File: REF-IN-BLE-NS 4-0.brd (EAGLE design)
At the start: 44 x 86 mm, 79 parts, among them U1 NRF52832_10QFN48, U2 AEM10941, X1 32 MHz, X2 32.768 kHz

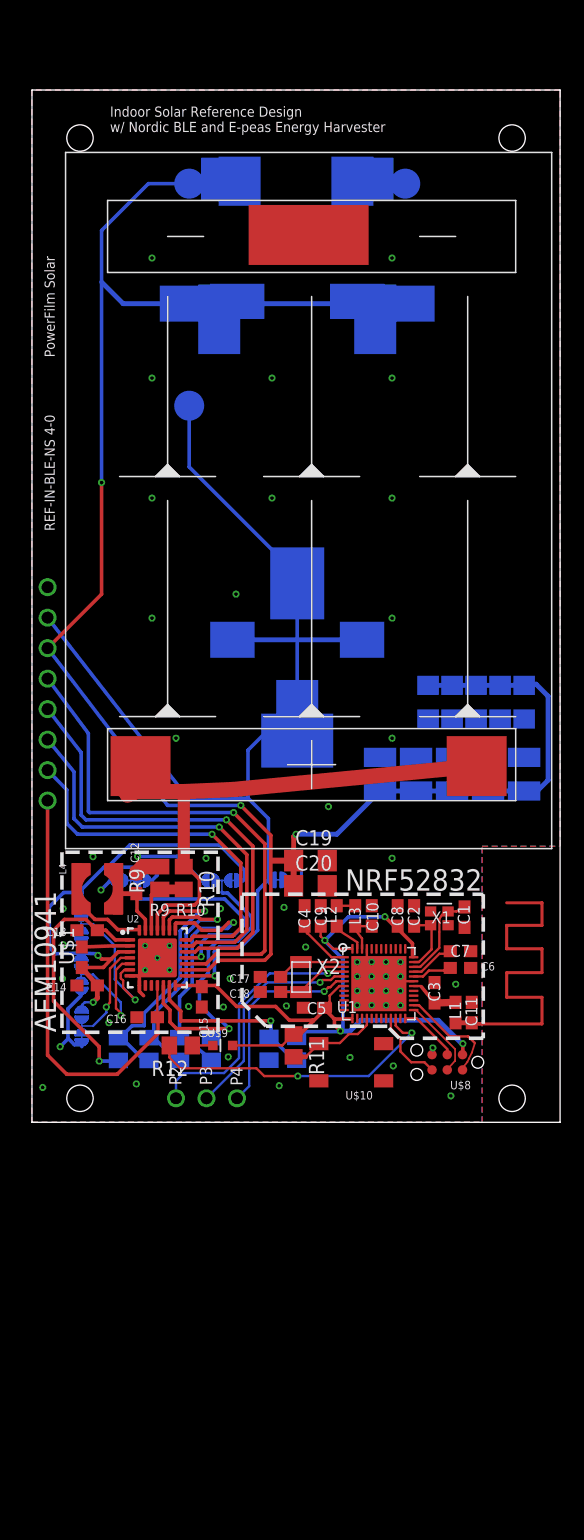
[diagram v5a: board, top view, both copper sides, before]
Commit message: Second revision of board Added LDO bypass circuit to attempt to get a higher efficiency from the charge capacitors. Added a way to break away solar from the rest of the assembly. Moved pin connectors to processing side of the board Swapped 0805 components for 0603 Moved the capacitor bank to the processing side of the board Rerouted some signals to fit everything nicely
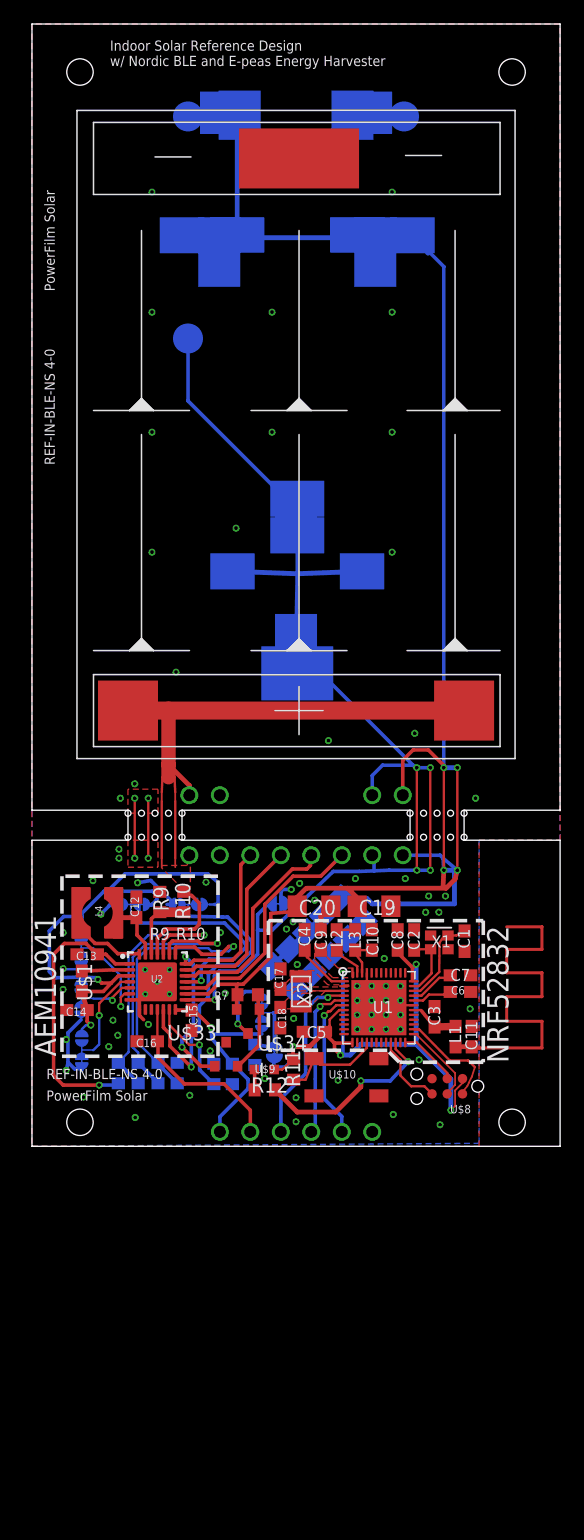
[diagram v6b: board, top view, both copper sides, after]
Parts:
- removed C26, C27, C28, C29, C30: (no value), resistor:C1210
- added R7: 1M, resistor:R0603
- added RTEST: (no value), resistor:R0603
- added U$31: (no value), 00_PF_Nordic:DOUBLE_SOLDER_BRIDGE_1_CLOSED
- added U$32: (no value), 00_PF_Nordic:SOLDER_BRIDGE_CLOSED
- added U$33: DMG2305U-13, 00-PF-DevKits:SOT-23-3-DIODESINC
- added U$34: DMG2302UK-13, 00_PF_Nordic:SOT-23-3-DIODESINC
- added U$35, U$36, U$37, U$38, U$39, U$40, U$41: N/A, 00_PF_Nordic:1MM_PAD
- AE1: value 2.4GHZ_ANTENNA -> N/A
- R1, R2, R3, R4, R5, R6, R9: device resistor:M0805 -> resistor:R0603
- R10, R11, R12: device resistor:R0805 -> resistor:R0603
- U$11: value SOLDER_BRIGDECLOSED -> (none)
- U$12, U$13, U$14, U$15, U$16, U$17, U$18, U$19, U$20, U$21, U$22: value 1MM_PAD -> N/A
- U$2, U$3, U$5, U$6: value DOUBLE_SOLDER_BRIDGE1_CLOSED -> (none)
- U$23: value CAP-XX_A-TYPE -> N/A
- U$24: value CAP-XX_S-TYPE -> N/A
- U$25: value CAP-XX_W-TYPE -> N/A
- U$26: value BZ01_L-TYPE -> N/A
- U$27: value BZ059_N-TYPE -> N/A
- U$28: value BZ01_S-TYPE -> N/A
- U$29: value BZ05_S-TYPE -> N/A
- U$30: value BZ09_S-TYPE -> N/A
- U$4: value DOUBLE_SOLDER_BRIDGE0_CLOSED -> N/A
- U$7: value SOLAR_CELL -> N/A
- U$8: value TC2030-IDC -> N/A
- moved U$18 34.3 mm to (30.9, 24.2)
- moved U$19 33.5 mm to (28.4, 24.2)
- moved U$16 32.4 mm to (18.2, 1.20)
- moved U$12 28.6 mm to (25.8, 24.2)
- moved C21 25.9 mm to (21.0, 14.0), turned to 225 degrees
- moved U$13 25.1 mm to (23.3, 24.2)
- moved C22 25.0 mm to (22.4, 15.4), turned to 225 degrees
- moved C23 24.1 mm to (23.8, 16.9), turned to 225 degrees
- moved C24 23.2 mm to (25.2, 18.3), turned to 225 degrees
- moved U$17 22.5 mm to (15.7, 29.2)
- moved C25 22.5 mm to (26.7, 19.7), turned to 225 degrees
- moved U$14 21.7 mm to (20.7, 24.2)
- moved U$15 18.3 mm to (18.2, 24.2)
- moved U$20 9.17 mm to (20.7, 1.20)
- moved U$21 9.17 mm to (23.3, 1.20)
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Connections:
- net N$33 renamed PRIM
- net N$39 renamed STATUS2
- net N$40 renamed STATUS1
- removed net N$41: U$15.P$1, U2.21
- new net N$34: C15.1, R6.2, U$31.IN0, U$37.P$1, U2.14
- new net N$45: RTEST.2, U$31.OUT, U$32.P$2
- new net N$46: U$31.IN1, U$33.3
- new net N$47: R7.1, U$33.1, U$34.2
- new net STATUS0: U$15.P$1, U$34.1, U2.21
- net BAL: now also U$41.P$1
- net BATT: now also R7.2, U$33.2, U$40.P$1; no longer C26.1, C27.1, C28.1, C29.1, C30.1
- net GND: now also RTEST.1, U$34.3, U$35.P$1, U$38.P$1; no longer C26.2, C27.2, C28.2, C29.2, C30.2
- net HVOUT: now also U$32.P$1; no longer C15.1, R6.2, U2.14
- net N$29: now also U$36.P$1, U$39.P$1
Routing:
- net N$41: track 31.5 -> 0.00 mm, vias 1 -> 0
- net STATUS0: track 0.00 -> 25.7 mm, vias 0 -> 2
- net PRIM: track 44.0 -> 20.0 mm, vias 1 -> 0
- net STATUS2: track 38.7 -> 17.5 mm, vias 1 -> 0
- net LVOUT: track 36.6 -> 15.5 mm
- net STATUS1: track 35.0 -> 15.1 mm, vias 1 -> 0
- net N$34: track 0.00 -> 18.6 mm, vias 0 -> 1
- net N$29: track 49.3 -> 67.4 mm
- net HVOUT: track 70.1 -> 53.5 mm, vias 4 -> 5
- net BAL: track 98.8 -> 112.2 mm, vias 1 -> 5
- net N$31: track 25.5 -> 16.0 mm
- net N$38: track 21.9 -> 14.7 mm
- net N$47: track 0.00 -> 6.77 mm
- net GND: track 34.5 -> 40.9 mm, vias 40 -> 64
- net N$26: track 9.71 -> 3.69 mm
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- added copper zone on layer 1, net HVOUT
- added copper zone on layer 1, net N$29
- added copper zone on layer 1, net N$36
- added copper zone on layer 1, net N$37
- added copper zone on layer 1, net N$48
- added copper zone on layer 1, net N$49
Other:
- board size 44 x 86 mm -> 44 x 93.5 mm
- board text added: "ENNRF"
- board text added: "HV"
- board text added: "LV"
- board text added: "PWRSRC"
- board text added: "RTEST"
- board text added: "S0"
- board text added: "S1"
- board text added: "S2"
- board text added: "SOL"
- board text removed: "1206"
- board text removed: "1210"
- board text removed: "LVOUT"
- board text removed: "STATUS0"
- board text removed: "STATUS1"
- board text removed: "STATUS2"
